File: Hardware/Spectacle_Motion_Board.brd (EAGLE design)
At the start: 25.4 x 55.9 mm, 49 parts, among them J1 FTDI_DEVICE, J10 AUDIO-JACK3, J3 USB-MICROB, J4 AUDIO-JACK3, U1 CY8C4146LQI-S422, U2 3.3V/150mA

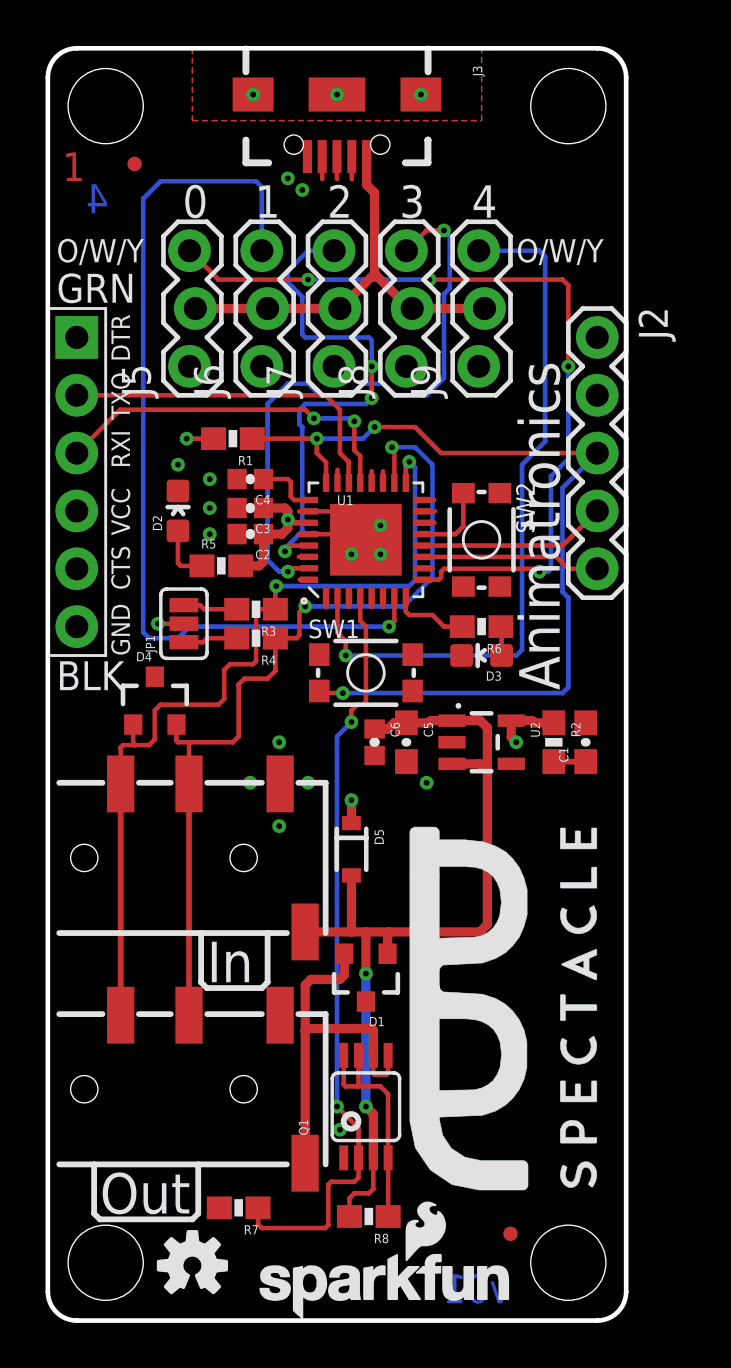
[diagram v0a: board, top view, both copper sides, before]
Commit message: Feedback from review incorporated, ready for qc review
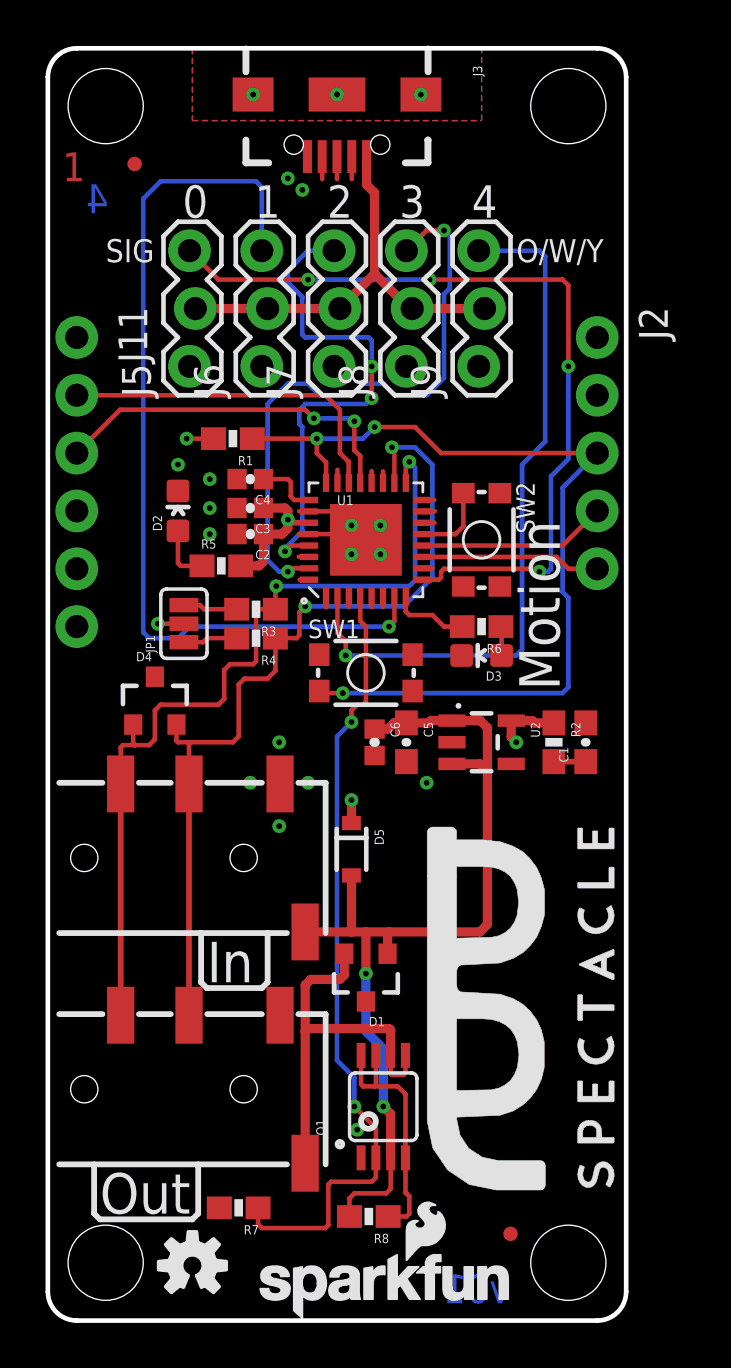
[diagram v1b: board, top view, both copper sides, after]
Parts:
- removed J1: FTDI_DEVICE, SparkFun-Connectors:FTDI_DEVICE_SIDE
- added J11: (no value), SparkFun-Connectors:1X06_NO_SILK
- J2: device SparkFun-Connectors:1X05 -> SparkFun-Connectors:1X05_NO_SILK
- J3: device SparkFun-Connectors:USB-B-MICRO-SMD_V03 -> SparkFun-Connectors:USB-B-MICRO-SMD_V03_RED_PASTE
- moved U$2 0.76 mm to (24.9, 5.71)
- moved Q1 0.76 mm to (14.7, 9.40)
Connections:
- net GND: now also J11.5, J11.6; no longer J1.P$5, J1.P$6
- net RXI: now also J11.3; no longer J1.P$3
- net TXO: now also J11.2; no longer J1.P$2
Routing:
- net V_OUT_EN: track 33.8 -> 34.9 mm
- net VIN: track 40.6 -> 41.7 mm
- net N$26: track 10.2 -> 11.1 mm
- net VOUT: track 18.3 -> 19.1 mm
- net GND: vias 15 -> 16
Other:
- board text added: "Motion"
- board text added: "SIG"
- board text removed: "Animatronics"

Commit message: Chg I2C pullup value
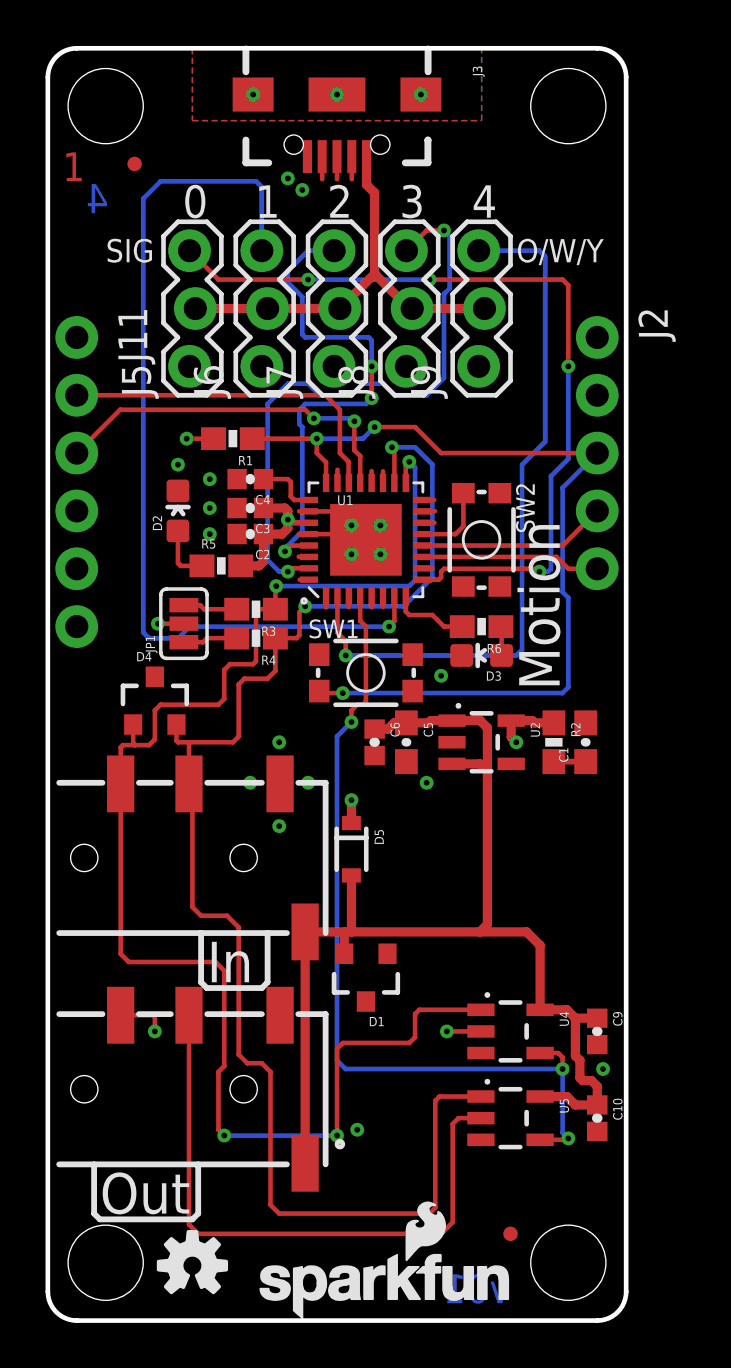
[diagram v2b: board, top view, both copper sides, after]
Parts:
- removed Q1: (no value), SparkFun-DiscreteSemi:MSOP8
- removed R7, R8: 10K, SparkFun-Resistors:0603-RES
- removed U$2: (no value), SparkFun-Aesthetics:SPECTACLE_LOGO_TITLE_0.35X0.70
- added C10, C9: 0.1uF, SparkFun-Capacitors:0402-CAP
- added U4, U5: SN74LVC1G66, SparkFun-AnalogIC:SOT23-5
- R3, R4: value 2.2k -> 4.7K
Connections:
- removed net N$26: Q1.4, Q1.7, Q1.8, R8.1
- removed net VOUT: D1.2, J10.EARTH, Q1.5, Q1.6
- removed net V_OUT_EN: Q1.2, R7.1, U1.4
- new net I2C_OUT_EN: U1.4, U4.4, U5.4
- new net SCL_OUT: J10.RING2, U4.2
- new net SDA_OUT: J10.RING1, U5.2
- net GND: now also C10.2, C9.2, U4.3, U5.3; no longer Q1.1, R7.2
- net SCL: now also U4.1; no longer J10.RING2
- net SDA: now also U5.1; no longer J10.RING1
- net VIN: now also C10.1, C9.1, D1.2, J10.EARTH, U4.5, U5.5; no longer D1.1, Q1.3, R8.2
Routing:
- net I2C_OUT_EN: track 0.00 -> 37.2 mm, vias 0 -> 3
- net V_OUT_EN: track 34.9 -> 0.00 mm, vias 2 -> 0
- net SDA_OUT: track 0.00 -> 26.8 mm
- net SCL: track 38.3 -> 64.3 mm, vias 2 -> 4
- net SDA: track 38.5 -> 63.8 mm
- net VOUT: track 19.1 -> 0.00 mm
- net SCL_OUT: track 0.00 -> 16.5 mm, vias 0 -> 2
- net VIN: track 41.7 -> 54.1 mm, vias 2 -> 0
- net N$26: track 11.1 -> 0.00 mm
- net GND: vias 16 -> 18

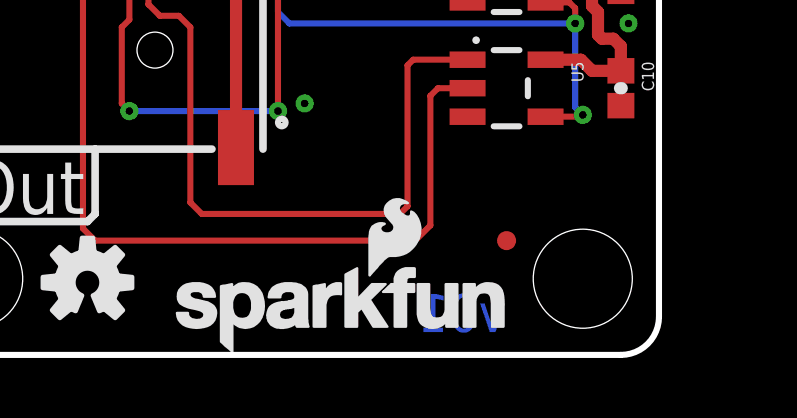
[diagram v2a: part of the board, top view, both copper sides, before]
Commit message: Feedback from reviews incorporated
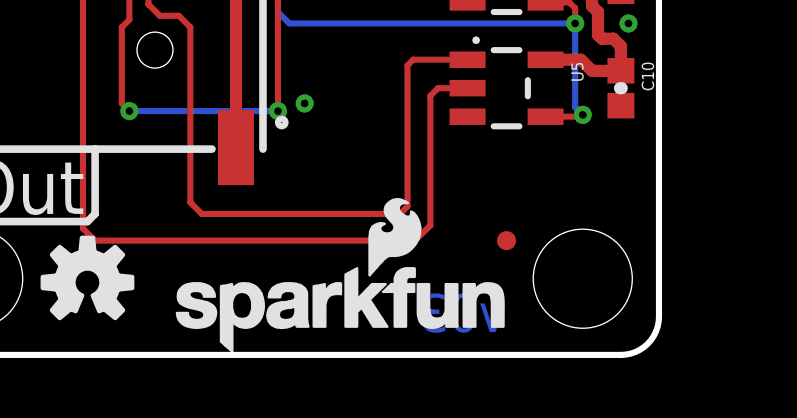
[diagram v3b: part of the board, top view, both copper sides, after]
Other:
- board text added: "v03"
- board text removed: "v01"
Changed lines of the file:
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@@
 <layers>
 <layer number="1" name="Top" color="4" fill="1" visible="yes" active="yes"/>
-<layer number="2" name="Route2" color="1" fill="3" visible="no" active="yes"/>
-<layer number="15" name="Route15" color="4" fill="6" visible="no" active="yes"/>
+<layer number="2" name="Route2" color="1" fill="3" visible="yes" active="yes"/>
+<layer number="15" name="Route15" color="4" fill="6" visible="yes" active="yes"/>
 <layer number="16" name="Bottom" color="1" fill="1" visible="yes" active="yes"/>
 <layer number="17" name="Pads" color="2" fill="1" visible="yes" active="yes"/>
@@
 <layer number="23" name="tOrigins" color="15" fill="1" visible="yes" active="yes"/>
 <layer number="24" name="bOrigins" color="15" fill="1" visible="yes" active="yes"/>
-<layer number="25" name="tNames" color="7" fill="1" visible="no" active="yes"/>
-<layer number="26" name="bNames" color="7" fill="1" visible="no" active="yes"/>
-<layer number="27" name="tValues" color="7" fill="1" visible="no" active="yes"/>
-<layer number="28" name="bValues" color="7" fill="1" visible="no" active="yes"/>
-<layer number="29" name="tStop" color="7" fill="3" visible="no" active="yes"/>
-<layer number="30" name="bStop" color="7" fill="6" visible="no" active="yes"/>
-<layer number="31" name="tCream" color="7" fill="4" visible="no" active="yes"/>
-<layer number="32" name="bCream" color="7" fill="5" visible="no" active="yes"/>
-<layer number="39" name="tKeepout" color="4" fill="11" visible="no" active="yes"/>
-<layer number="40" name="bKeepout" color="1" fill="11" visible="no" active="yes"/>
-<layer number="41" name="tRestrict" color="4" fill="10" visible="no" active="yes"/>
-<layer number="42" name="bRestrict" color="1" fill="10" visible="no" active="yes"/>
-<layer number="43" name="vRestrict" color="2" fill="10" visible="no" active="yes"/>
-<layer number="44" name="Drills" color="7" fill="1" visible="no" active="yes"/>
+<layer number="25" name="tNames" color="7" fill="1" visible="yes" active="yes"/>
+<layer number="26" name="bNames" color="7" fill="1" visible="yes" active="yes"/>
+<layer number="27" name="tValues" color="7" fill="1" visible="yes" active="yes"/>
+<layer number="28" name="bValues" color="7" fill="1" visible="yes" active="yes"/>
+<layer number="29" name="tStop" color="7" fill="3" visible="yes" active="yes"/>
+<layer number="30" name="bStop" color="7" fill="6" visible="yes" active="yes"/>
+<layer number="31" name="tCream" color="7" fill="4" visible="yes" active="yes"/>
+<layer number="32" name="bCream" color="7" fill="5" visible="yes" active="yes"/>
+<layer number="39" name="tKeepout" color="4" fill="11" visible="yes" active="yes"/>
+<layer number="40" name="bKeepout" color="1" fill="11" visible="yes" active="yes"/>
+<layer number="41" name="tRestrict" color="4" fill="10" visible="yes" active="yes"/>
+<layer number="42" name="bRestrict" color="1" fill="10" visible="yes" active="yes"/>
+<layer number="43" name="vRestrict" color="2" fill="10" visible="yes" active="yes"/>
+<layer number="44" name="Drills" color="7" fill="1" visible="yes" active="yes"/>
 <layer number="45" name="Holes" color="7" fill="1" visible="yes" active="yes"/>
-<layer number="46" name="Milling" color="3" fill="1" visible="no" active="yes"/>
-<layer number="47" name="Measures" color="7" fill="1" visible="no" active="yes"/>
-<layer number="48" name="Document" color="7" fill="1" visible="no" active="yes"/>
-<layer number="49" name="Reference" color="7" fill="1" visible="no" active="yes"/>
+<layer number="46" name="Milling" color="3" fill="1" visible="yes" active="yes"/>
+<layer number="47" name="Measures" color="7" fill="1" visible="yes" active="yes"/>
+<layer number="48" name="Document" color="7" fill="1" visible="yes" active="yes"/>
+<layer number="49" name="Reference" color="7" fill="1" visible="yes" active="yes"/>
 <layer number="51" name="tDocu" color="6" fill="1" visible="yes" active="yes"/>
-<layer number="52" name="bDocu" color="7" fill="1" visible="no" active="yes"/>
+<layer number="52" name="bDocu" color="7" fill="1" visible="yes" active="yes"/>
 <layer number="3" name="Route3" color="4" fill="3" visible="no" active="no"/>
 <layer number="4" name="Route4" color="1" fill="4" visible="no" active="no"/>
@@
 <text x="19.177" y="49.149" size="1.4224" layer="21" font="vector" ratio="15" align="center">4</text>
 <text x="90.17" y="45.72" size="1.778" layer="51" font="vector" ratio="15">Mike Hord</text>
-<text x="20.32" y="0.762" size="1.27" layer="16" font="vector" ratio="15" rot="MR0">v01</text>
+<text x="20.32" y="0.762" size="1.27" layer="16" font="vector" ratio="15" rot="MR0">v03</text>
 <text x="0.635" y="50.038" size="1.27" layer="1" font="vector" ratio="15">1</text>
 <text x="1.778" y="50.038" size="1.27" layer="2" font="vector" ratio="15">2</text>
